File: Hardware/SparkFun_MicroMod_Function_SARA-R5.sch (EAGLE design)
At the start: 94 parts, among them J1 MICROMOD_FUNCTION_STANDARD, J2 U.FL, J4 U.FL, J9 NANO_SIM, Q2 310mA/60V/1.6Ω, Q3 310mA/60V/1.6Ω, Q5 310mA/60V/1.6Ω, Q6 310mA/60V/1.6Ω, U1 SARA-R510M8S, U11 74HC1G04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

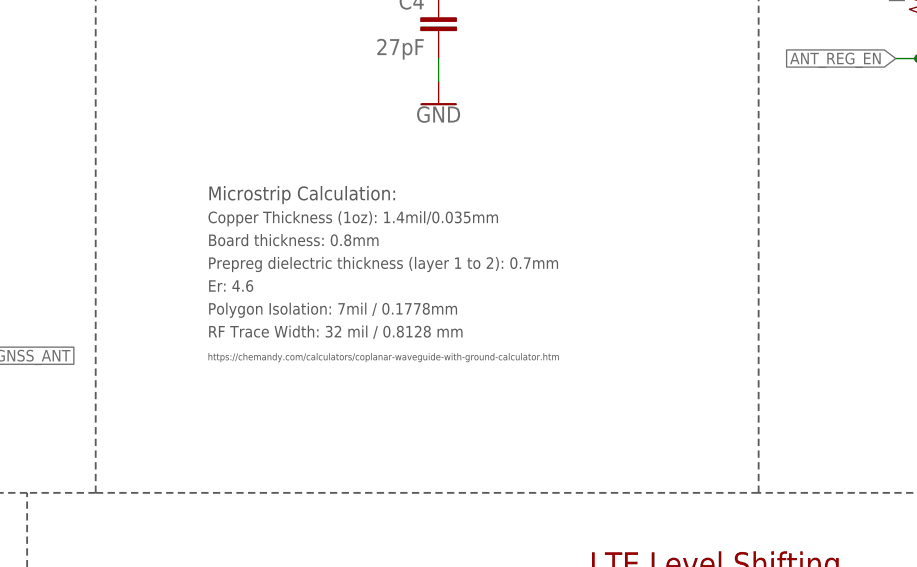
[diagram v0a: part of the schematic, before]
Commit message: RF traces corrected to 12.3mil
-also updated calc paragraph in SCH
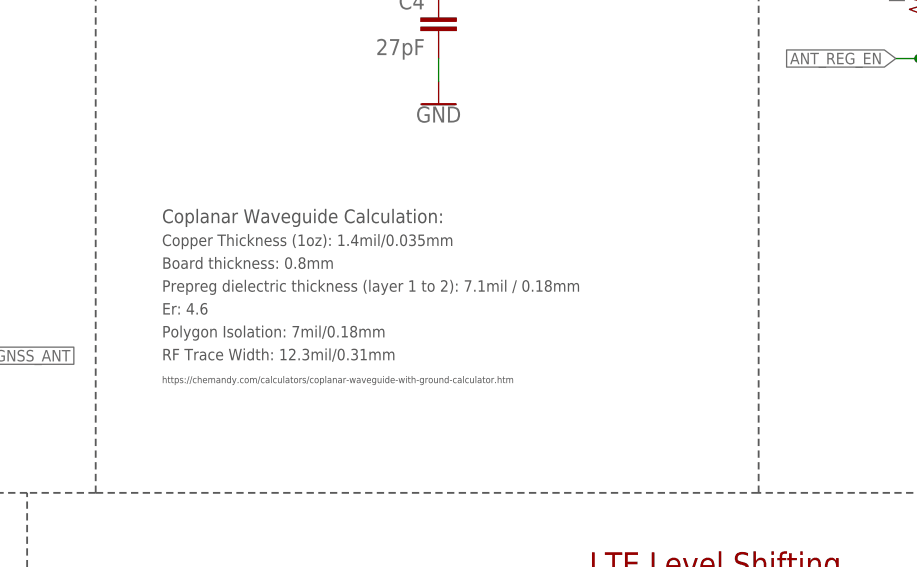
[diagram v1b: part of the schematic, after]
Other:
- note added: "Coplanar Waveguide Calculation:"
- note added: "Polygon Isolation: 7mil/0.18mm"
- note added: "Prepreg dielectric thickness (layer 1 to 2): 7.1mil / 0.18mm"
- note added: "RF Trace Width: 12.3mil/0.31mm"
- note removed: "Microstrip Calculation:"
- note removed: "Polygon Isolation: 7mil / 0.1778mm"
- note removed: "Prepreg dielectric thickness (layer 1 to 2): 0.7mm"
- note removed: "RF Trace Width: 32 mil / 0.8128 mm"
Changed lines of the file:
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@@
 <class number="2" name="supply" width="0.4064" drill="0">
 </class>
-<class number="3" name="RF" width="0.8128" drill="0">
+<class number="3" name="RF" width="0.31241875" drill="0">
 <clearance class="3" value="0.1778"/>
 </class>
@@
 <wire x1="330.2" y1="147.32" x2="330.2" y2="142.24" width="0.6096" layer="97"/>
 <wire x1="127" y1="55.88" x2="0" y2="55.88" width="0.2032" layer="97" style="longdash"/>
-<text x="274.066" y="195.072" size="1.27" layer="97" font="vector">Board thickness: 0.8mm</text>
-<text x="274.066" y="189.992" size="1.27" layer="97" font="vector">Er: 4.6</text>
-<text x="274.066" y="197.612" size="1.27" layer="97" font="vector">Copper Thickness (1oz): 1.4mil/0.035mm</text>
-<text x="274.066" y="184.912" size="1.27" layer="97" font="vector">RF Trace Width: 32 mil / 0.8128 mm</text>
-<text x="274.066" y="187.452" size="1.27" layer="97" font="vector">Polygon Isolation: 7mil / 0.1778mm</text>
-<text x="274.066" y="192.532" size="1.27" layer="97" font="vector">Prepreg dielectric thickness (layer 1 to 2): 0.7mm</text>
-<text x="274.066" y="182.372" size="0.762" layer="97" font="vector">https://chemandy.com/calculators/coplanar-waveguide-with-ground-calculator.htm</text>
-<text x="274.066" y="200.152" size="1.524" layer="97" font="vector" ratio="15">Microstrip Calculation:</text>
 <text x="190.754" y="159.766" size="2.54" layer="94" font="vector" align="center">USB</text>
 <wire x1="431.8" y1="167.64" x2="335.28" y2="167.64" width="0.2032" layer="97" style="longdash"/>
@@
 Closed (default): connected to GND</text>
 <wire x1="144.272" y1="115.062" x2="148.082" y2="101.346" width="0.2032" layer="97" style="shortdash"/>
+<text x="268.986" y="192.532" size="1.27" layer="97" font="vector">Board thickness: 0.8mm</text>
+<text x="268.986" y="187.452" size="1.27" layer="97" font="vector">Er: 4.6</text>
+<text x="268.986" y="195.072" size="1.27" layer="97" font="vector">Copper Thickness (1oz): 1.4mil/0.035mm</text>
+<text x="268.986" y="182.372" size="1.27" layer="97" font="vector">RF Trace Width: 12.3mil/0.31mm</text>
+<text x="268.986" y="184.912" size="1.27" layer="97" font="vector">Polygon Isolation: 7mil/0.18mm</text>
+<text x="268.986" y="189.992" size="1.27" layer="97" font="vector">Prepreg dielectric thickness (layer 1 to 2): 7.1mil / 0.18mm</text>
+<text x="268.986" y="179.832" size="0.762" layer="97" font="vector">https://chemandy.com/calculators/coplanar-waveguide-with-ground-calculator.htm</text>
+<text x="268.986" y="197.612" size="1.524" layer="97" font="vector" ratio="15">Coplanar Waveguide Calculation:</text>
 </plain>
 <instances>

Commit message: LED disable jumpers added
-LTE_RI_LED, LTE_NI_LED, LTE_ON
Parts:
- added LTE_NI_LED, LTE_ON_LED, LTE_RI_LED: JUMPER-SMT_2_NC_TRACE_SILK, SparkFun-Jumpers:JUMPER-SMT_2_NC_TRACE_SILK
- FD1, FD2, FD3, FD4: value FIDUCIAL1X2 -> FIDUCIALUFIDUCIAL; device SparkFun-Aesthetics:FIDUCIAL1X2 -> SparkFun-Aesthetics:FIDUCIALUFIDUCIAL
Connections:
- new net N$19: D18.A, LTE_NI_LED.1
- new net N$20: LTE_RI_LED.1, R43.1
- new net N$21: D17.A, LTE_ON_LED.1
- net 3.3V: now also LTE_NI_LED.2, LTE_ON_LED.2; no longer D17.A, D18.A
- net LTE_18_RI: now also LTE_RI_LED.2; no longer R43.1

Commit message: add 0.1uF cap on VCCB for level shifter
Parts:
- added C5: 0.1uF, SparkFun-Capacitors:0.1UF-0402-16V-10%
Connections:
- net 3.3V: now also C5.1
- net GND: now also C5.2
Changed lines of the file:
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@@
 <part name="SUPPLY22" library="SparkFun-PowerSymbols" deviceset="3.3V" device=""/>
 <part name="SUPPLY4" library="SparkFun-PowerSymbols" deviceset="3.3V" device=""/>
+<part name="SUPPLY10" library="SparkFun-PowerSymbols" deviceset="3.3V" device=""/>
+<part name="C5" library="SparkFun-Capacitors" library_urn="urn:adsk.eagle:library:510" deviceset="0.1UF" device="-0402-16V-10%" package3d_urn="urn:adsk.eagle:package:37413/1" value="0.1uF"/>
+<part name="GND28" library="SparkFun-PowerSymbols" deviceset="GND" device=""/>
 </parts>
 <sheets>
@@
 <attribute name="VALUE" x="292.1" y="61.214" size="1.778" layer="96" font="vector" align="bottom-center"/>
 </instance>
+<instance part="SUPPLY10" gate="G$1" x="314.96" y="101.6" smashed="yes">
+<attribute name="VALUE" x="314.96" y="104.394" size="1.778" layer="96" font="vector" align="bottom-center"/>
+</instance>
+<instance part="C5" gate="G$1" x="314.96" y="93.98" smashed="yes" rot="MR0">
+<attribute name="NAME" x="316.484" y="96.774" size="1.778" layer="95" font="vector"/>
+<attribute name="VALUE" x="316.23" y="91.948" size="1.778" layer="96" font="vector"/>
+</instance>
+<instance part="GND28" gate="1" x="314.96" y="86.36" smashed="yes">
+<attribute name="VALUE" x="314.96" y="86.106" size="1.778" layer="96" font="vector" align="top-center"/>
+</instance>
 </instances>
 <busses>
@@
 <wire x1="294.64" y1="55.88" x2="292.1" y2="55.88" width="0.1524" layer="91"/>
 </segment>
+<segment>
+<pinref part="SUPPLY10" gate="G$1" pin="3.3V"/>
+<pinref part="C5" gate="G$1" pin="1"/>
+<wire x1="314.96" y1="101.6" x2="314.96" y2="99.06" width="0.1524" layer="91"/>
+</segment>
 </net>
 <net name="GND" class="0">
@@
 <wire x1="180.34" y1="134.62" x2="182.88" y2="134.62" width="0.1524" layer="91"/>
 </segment>
+<segment>
+<pinref part="C5" gate="G$1" pin="2"/>
+<pinref part="GND28" gate="1" pin="GND"/>
+<wire x1="314.96" y1="88.9" x2="314.96" y2="91.44" width="0.1524" layer="91"/>
+</segment>
 </net>

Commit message: Library work and BOM consolidation
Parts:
- C17, C19, C25, C32, C36, C5, C9: device SparkFun-Capacitors:0.1UF-0402-16V-10% -> SparkFun-Capacitors:0.1UF-0402T-16V-10%
- C2: device SparkFun-Capacitors:0.1UF-0603-25V-(+80/-20%) -> SparkFun-Capacitors:0.1UF-0402T-16V-10%
- C24: device HPG_Solution:8.2PF-0603-50V-10% -> SparkFun-Capacitors:8.2PF-0603-50V-10%
- C28: device SparkFun-Capacitors:4.7UF0603 -> SparkFun-Capacitors:4.7UF-0603-6.3V-(10%)
- J9: device HPG_Solution_v1.0:SIMHOLDER-PUSHPUSH -> SparkFun-Connectors:SIMHOLDER_WITH_CD-PUSHPUSH
- R23: device SparkFun-Resistors:10KOHM-0603-1/10W-1% -> SparkFun-Resistors:10KOHM-0402T-1/16W-1%

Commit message: added PTC fuse to USB input
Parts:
- added F2: 6V/2A, SparkFun-Fuses:PPTC_6V2A
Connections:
- new net N$22: F2.1, J3.VBUS
- net V_USB: now also F2.2; no longer J3.VBUS
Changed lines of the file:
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@@
 <part name="FRAME2" library="SparkFun-Aesthetics" deviceset="FRAME-LEDGER" device=""/>
 <part name="D2" library="SparkFun-DiscreteSemi" deviceset="DIODE-SCHOTTKY" device="-BAT60A" value="3A/10V/280mV"/>
-<part name="SUPPLY19" library="SparkFun-PowerSymbols" deviceset="V_USB" device=""/>
 <part name="SUPPLY20" library="SparkFun-PowerSymbols" deviceset="V_USB" device=""/>
 <part name="D1" library="SparkFun-DiscreteSemi" deviceset="DIODE-SCHOTTKY" device="-BAT60A" value="3A/10V/280mV"/>
@@
 <part name="C5" library="SparkFun-Capacitors" deviceset="0.1UF" device="-0402T-16V-10%" value="0.1uF"/>
 <part name="GND28" library="SparkFun-PowerSymbols" deviceset="GND" device=""/>
+<part name="F2" library="SparkFun-Fuses" deviceset="PPTC" device="_6V2A" value="6V/2A"/>
+<part name="SUPPLY23" library="SparkFun-PowerSymbols" deviceset="V_USB" device=""/>
 </parts>
 <sheets>
@@
 <attribute name="VALUE" x="22.86" y="247.904" size="1.016" layer="96" font="vector" rot="MR90" align="top-left"/>
 </instance>
-<instance part="SUPPLY19" gate="G$1" x="154.94" y="144.78" smashed="yes">
-<attribute name="VALUE" x="154.94" y="147.574" size="1.778" layer="96" font="vector" align="bottom-center"/>
-</instance>
 <instance part="SUPPLY20" gate="G$1" x="10.16" y="259.08" smashed="yes">
 <attribute name="VALUE" x="10.16" y="261.874" size="1.778" layer="96" font="vector" align="bottom-center"/>
@@
 <instance part="GND28" gate="1" x="314.96" y="86.36" smashed="yes">
 <attribute name="VALUE" x="314.96" y="86.106" size="1.778" layer="96" font="vector" align="top-center"/>
+</instance>
+<instance part="F2" gate="F1" x="162.56" y="144.78" smashed="yes">
+<attribute name="NAME" x="163.322" y="146.558" size="1.778" layer="95" font="vector" align="bottom-center"/>
+<attribute name="VALUE" x="163.068" y="142.494" size="1.778" layer="96" font="vector" align="top-center"/>
+</instance>
+<instance part="SUPPLY23" gate="G$1" x="172.72" y="147.32" smashed="yes">
+<attribute name="VALUE" x="172.72" y="150.114" size="1.778" layer="96" font="vector" align="bottom-center"/>
 </instance>
 </instances>
@@
 <net name="V_USB" class="0">
 <segment>
-<pinref part="J3" gate="J1" pin="VBUS"/>
-<pinref part="SUPPLY19" gate="G$1" pin="V_USB"/>
-<wire x1="152.4" y1="142.24" x2="154.94" y2="142.24" width="0.1524" layer="91"/>
-<wire x1="154.94" y1="142.24" x2="154.94" y2="144.78" width="0.1524" layer="91"/>
-</segment>
-<segment>
 <pinref part="D1" gate="G$1" pin="A"/>
 <pinref part="SUPPLY20" gate="G$1" pin="V_USB"/>
@@
 <wire x1="205.74" y1="134.62" x2="205.74" y2="142.24" width="0.1524" layer="91"/>
 <pinref part="D6" gate="D1" pin="5"/>
+</segment>
+<segment>
+<pinref part="SUPPLY23" gate="G$1" pin="V_USB"/>
+<wire x1="170.18" y1="144.78" x2="172.72" y2="144.78" width="0.1524" layer="91"/>
+<wire x1="172.72" y1="144.78" x2="172.72" y2="147.32" width="0.1524" layer="91"/>
+<pinref part="F2" gate="F1" pin="2"/>
 </segment>
 </net>
@@
 </segment>
 </net>
+<net name="N$22" class="0">
+<segment>
+<pinref part="J3" gate="J1" pin="VBUS"/>
+<wire x1="152.4" y1="142.24" x2="154.94" y2="142.24" width="0.1524" layer="91"/>
+<wire x1="154.94" y1="142.24" x2="154.94" y2="144.78" width="0.1524" layer="91"/>
+<pinref part="F2" gate="F1" pin="1"/>
+<wire x1="154.94" y1="144.78" x2="157.48" y2="144.78" width="0.1524" layer="91"/>
+</segment>
+</net>

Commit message: LTE_RESET changed to 10K
-LTE_RESET was not working with 100K, so changed to 10K
-Moved ANT regulator power control to different F pin, to avoid RX/TX sharing conflict
-corrected SCH text note about shared pins for RX1/TX1 on esp32
-corrected RTS1/CTS1 back so they are not swapped on this FB.
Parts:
- R5: value 100k -> 10k; device SparkFun-Resistors:100KOHM-0402T-1/16W-1% -> SparkFun-Resistors:10KOHM-0402T-1/16W-1%
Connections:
- net LTE_18_CTS: now also U2.A4; no longer U2.A3
- net LTE_18_RTS: now also U2.A3; no longer U2.A4
- net N$4: now also J1.F7; no longer J1.F4
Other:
- note added: "F3/F4 are shared with RX/TX on ESP32"
- note removed: "F6/F7 are shared with RX/TX on ESP32"
- moved on the sheet: ANT_REG_EN
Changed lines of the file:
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@@
 <part name="LOGO1" library="SparkFun-Aesthetics" deviceset="SFE_LOGO_NAME_FLAME" device=".2_INCH"/>
 <part name="LOGO2" library="SparkFun-Aesthetics" deviceset="SFE_LOGO_FLAME" device=".2_INCH" value="SFE_LOGO_FLAME.2_INCH"/>
-<part name="R5" library="SparkFun-Resistors" deviceset="100KOHM" device="-0402T-1/16W-1%" value="100k"/>
+<part name="R5" library="SparkFun-Resistors" deviceset="10KOHM" device="-0402T-1/16W-1%" value="10k"/>
 <part name="SUPPLY16" library="SparkFun-PowerSymbols" deviceset="3.3V" device=""/>
 <part name="SUPPLY2" library="SparkFun-PowerSymbols" deviceset="VCCIO" device=""/>
@@
 <wire x1="254" y1="78.74" x2="254" y2="167.64" width="0.2032" layer="97" style="longdash"/>
 <wire x1="218.44" y1="0" x2="218.44" y2="78.74" width="0.2032" layer="97" style="longdash"/>
-<text x="92.71" y="89.662" size="1.778" layer="97" font="vector">F6/F7 are shared
+<text x="92.71" y="71.882" size="1.778" layer="97" font="vector">F3/F4 are shared
 with RX/TX on ESP32</text>
 <text x="332.994" y="6.604" size="2.54" layer="94" font="vector">Revised by: Pete Lewis</text>
@@
 <attribute name="NAME" x="408.94" y="222.25" size="1.778" layer="95" font="vector"/>
 </instance>
-<instance part="ANT_REG_EN" gate="G$1" x="99.06" y="99.06" smashed="yes" rot="R180">
-<attribute name="NAME" x="100.838" y="99.314" size="1.27" layer="95" font="vector"/>
+<instance part="ANT_REG_EN" gate="G$1" x="99.06" y="91.44" smashed="yes" rot="R180">
+<attribute name="NAME" x="100.838" y="91.694" size="1.27" layer="95" font="vector"/>
 </instance>
 <instance part="R2" gate="G$1" x="353.06" y="223.52" smashed="yes" rot="R90">
@@
 </segment>
 </net>
+<net name="LTE_18_CTS" class="0">
+<segment>
+<label x="269.24" y="114.3" size="1.27" layer="95" font="vector" rot="R180" xref="yes"/>
+<wire x1="276.86" y1="114.3" x2="269.24" y2="114.3" width="0.1524" layer="91"/>
+<pinref part="U2" gate="G$1" pin="A4"/>
+</segment>
+<segment>
+<wire x1="208.28" y1="231.14" x2="205.74" y2="231.14" width="0.1524" layer="91"/>
+<label x="205.74" y="231.14" size="1.27" layer="95" font="vector" rot="R180" xref="yes"/>
+<pinref part="U1" gate="G$2" pin="CTS_O"/>
+</segment>
+</net>
 <net name="LTE_18_RTS" class="0">
+<segment>
+<label x="269.24" y="116.84" size="1.27" layer="95" font="vector" rot="R180" xref="yes"/>
+<wire x1="276.86" y1="116.84" x2="269.24" y2="116.84" width="0.1524" layer="91"/>
+<pinref part="U2" gate="G$1" pin="A3"/>
+</segment>
 <segment>
 <wire x1="208.28" y1="233.68" x2="205.74" y2="233.68" width="0.1524" layer="91"/>
 <label x="205.74" y="233.68" size="1.27" layer="95" font="vector" rot="R180" xref="yes"/>
 <pinref part="U1" gate="G$2" pin="RTS_I"/>
-</segment>
-<segment>
-<label x="269.24" y="114.3" size="1.27" layer="95" font="vector" rot="R180" xref="yes"/>
-<wire x1="276.86" y1="114.3" x2="269.24" y2="114.3" width="0.1524" layer="91"/>
-<pinref part="U2" gate="G$1" pin="A4"/>
-</segment>
-</net>
-<net name="LTE_18_CTS" class="0">
-<segment>
-<wire x1="208.28" y1="231.14" x2="205.74" y2="231.14" width="0.1524" layer="91"/>
-<label x="205.74" y="231.14" size="1.27" layer="95" font="vector" rot="R180" xref="yes"/>
-<pinref part="U1" gate="G$2" pin="CTS_O"/>
-</segment>
-<segment>
-<label x="269.24" y="116.84" size="1.27" layer="95" font="vector" rot="R180" xref="yes"/>
-<wire x1="276.86" y1="116.84" x2="269.24" y2="116.84" width="0.1524" layer="91"/>
-<pinref part="U2" gate="G$1" pin="A3"/>
 </segment>
 </net>
@@
 </segment>
 <segment>
-<wire x1="104.14" y1="99.06" x2="111.76" y2="99.06" width="0.1524" layer="91"/>
-<label x="111.76" y="99.06" size="1.27" layer="95" font="vector" xref="yes"/>
+<wire x1="104.14" y1="91.44" x2="111.76" y2="91.44" width="0.1524" layer="91"/>
+<label x="111.76" y="91.44" size="1.27" layer="95" font="vector" xref="yes"/>
 <pinref part="ANT_REG_EN" gate="G$1" pin="1"/>
 </segment>
@@
 <segment>
 <pinref part="ANT_REG_EN" gate="G$1" pin="2"/>
-<pinref part="J1" gate="J1" pin="F4"/>
-<wire x1="93.98" y1="99.06" x2="91.44" y2="99.06" width="0.1524" layer="91"/>
-</segment>
-</net>
+<pinref part="J1" gate="J1" pin="F7"/>
+<wire x1="93.98" y1="91.44" x2="91.44" y2="91.44" width="0.1524" layer="91"/>
+</segment>
+</net>
